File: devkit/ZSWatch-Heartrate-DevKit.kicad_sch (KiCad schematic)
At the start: 0 parts

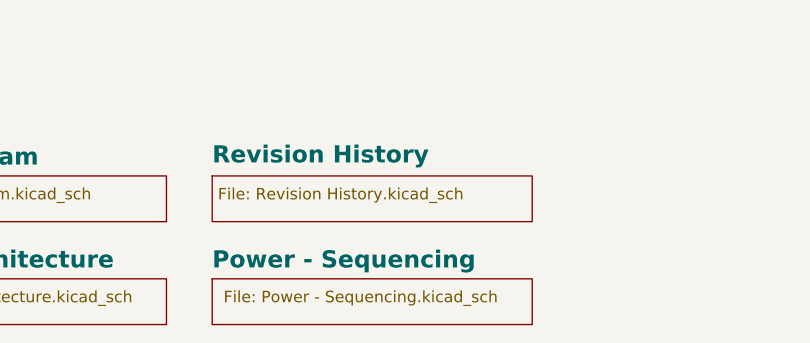
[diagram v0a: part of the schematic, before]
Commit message: Prepare release
- Set variant to CHECKED
- Remove unused files
- Fix ERC errors
- Fix DRC errors
- Fix different documentation errors
- Fix different path errors for the release build
- Remove Power Sequencing page
- Add PDF_REPORT_ROOT_DIR variable to build
- Add script for CHANGELOG generation

Signed-off-by: Daniel Kampert <DanielKampert@kampis-elektroecke.de>
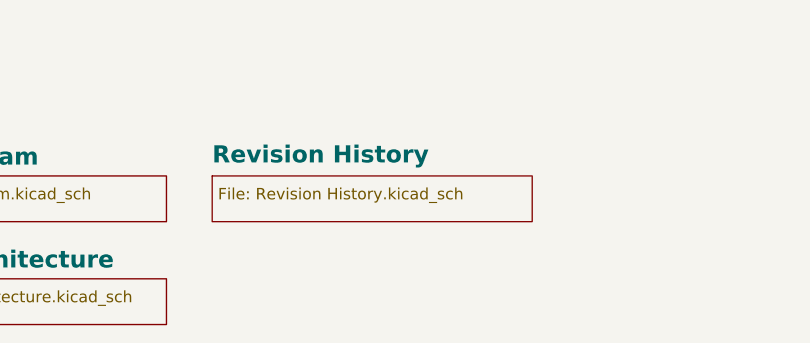
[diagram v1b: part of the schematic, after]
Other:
- removed sheet Power - Sequencing
- title: Dock-HW -> Heartrate-DevKit-HW
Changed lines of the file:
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@@
 	(paper "A3")
 	(title_block
-		(title "Dock-HW")
+		(title "Heartrate-DevKit-HW")
 		(date "2025-07-13")
 		(rev "${REVISION}")
@@
 			(type dot)
 			(color 0 0 0 1)
-		)
-	)
-	(sheet
-		(at 346.71 314.96)
-		(size 35.56 5.08)
-		(exclude_from_sim no)
-		(in_bom yes)
-		(on_board yes)
-		(dnp no)
-		(stroke
-			(width 0.1524)
-			(type solid)
-		)
-		(fill
-			(color 0 0 0 0.0000)
-		)
-		(property "Sheetname" "Power - Sequencing"
-			(at 346.71 313.9309 0)
-			(effects
-				(font
-					(face "Times New Roman")
-					(size 1.905 1.905)
-					(bold yes)
-					(color 0 0 0 1)
-				)
-				(justify left bottom)
-			)
-		)
-		(property "Sheetfile" "Power - Sequencing.kicad_sch"
-			(at 347.98 316.23 0)
-			(effects
-				(font
-					(face "Arial")
-					(size 1.27 1.27)
-				)
-				(justify left top)
-			)
-		)
-		(instances
-			(project "KDT_Hierarchical_KiBot"
-				(path "/f9e05184-c88b-4a88-ae9c-ab2bdb32be7c"
-					(page "6")
-				)
-			)
-			(project "ZSWatch-HeartRate"
-				(path "/d5742f03-3b1a-42e5-a384-018bd4b919aa"
-					(page "5")
-				)
-			)
 		)
 	)
@@
 			(project "ZSWatch-HeartRate"
 				(path "/d5742f03-3b1a-42e5-a384-018bd4b919aa"
-					(page "6")
+					(page "5")
 				)
 			)
